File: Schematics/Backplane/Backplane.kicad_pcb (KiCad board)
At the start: 2 copper layers, 69.5 x 98.5 mm, 21 parts, among them J1 Edge Connector (SLOT 1), J2 Edge Connector (SLOT 2), J3 Edge Connector (SLOT 3), J4 Edge Connector (SLOT 4), J5 Edge Connector (SLOT 5), J6 Conn_01x06_Socket

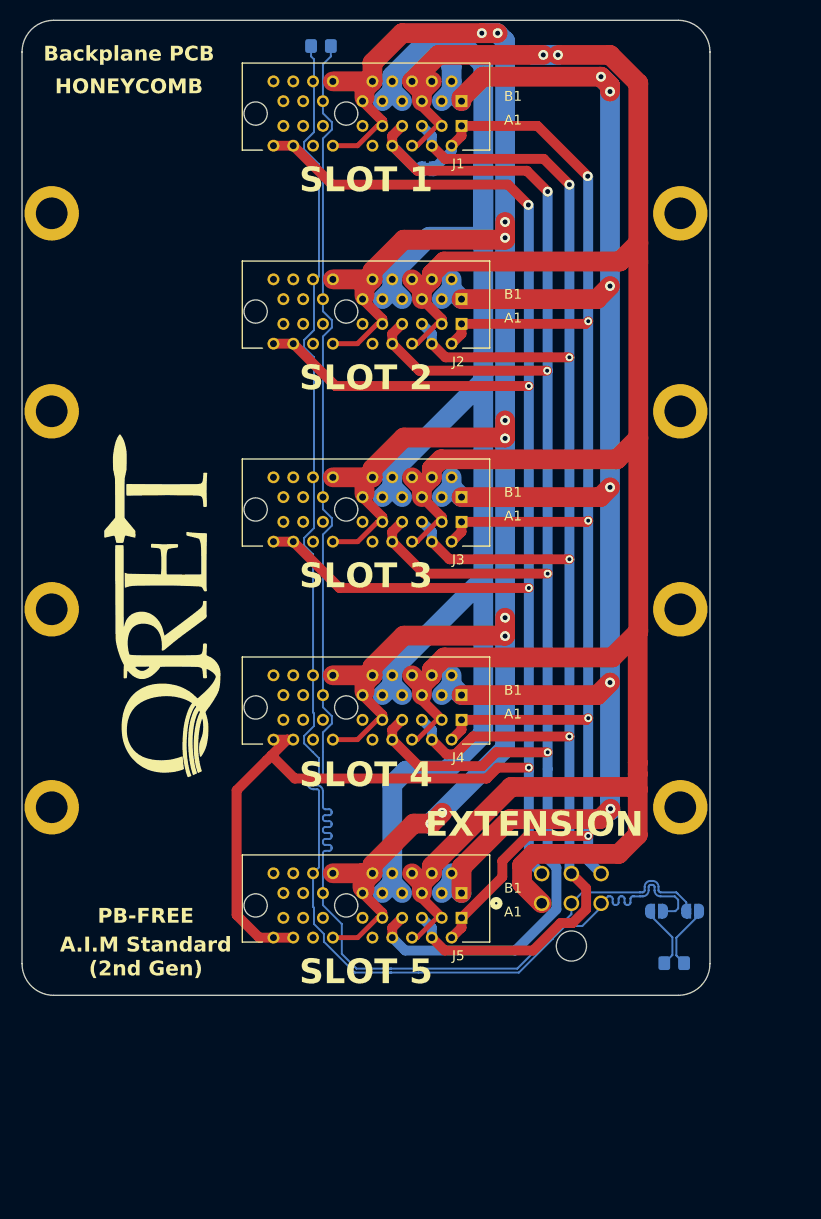
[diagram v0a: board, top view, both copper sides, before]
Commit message: restored non hybrid backplane
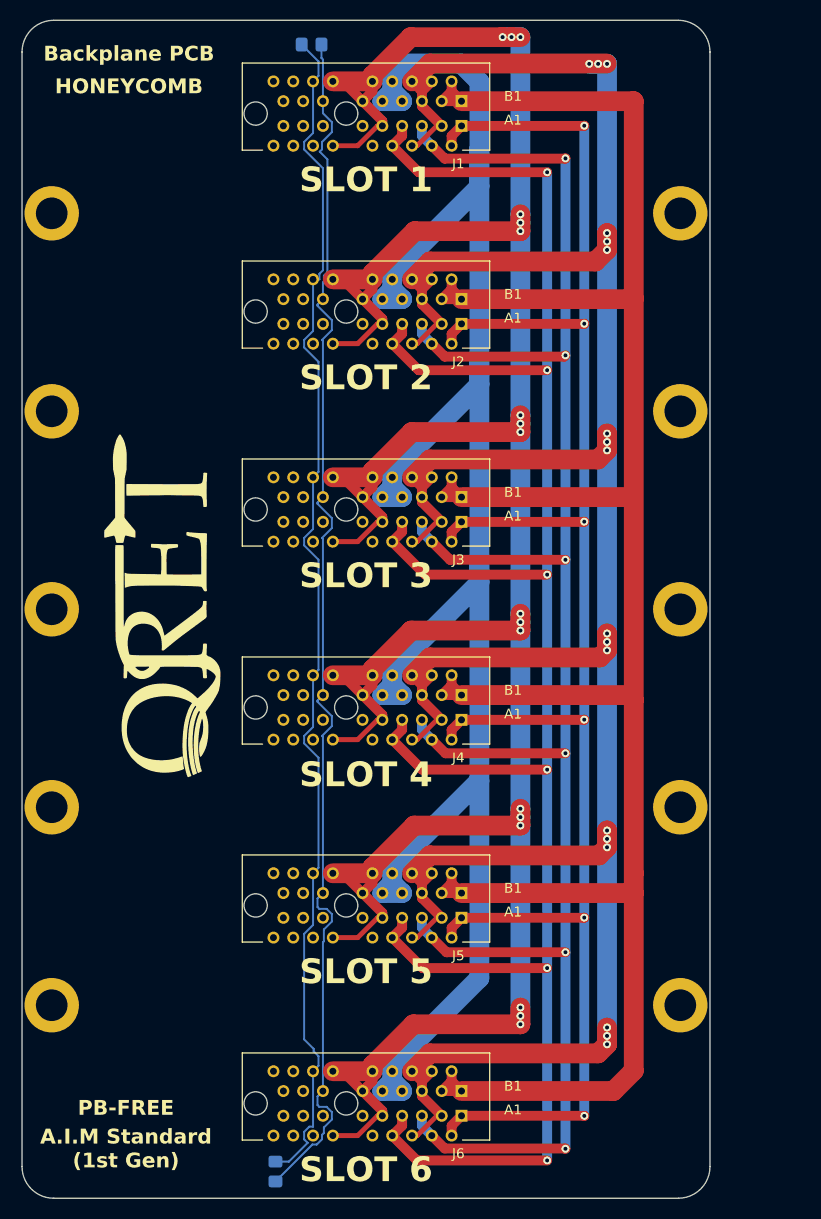
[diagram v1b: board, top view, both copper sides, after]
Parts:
- removed JP1, JP2: SolderJumper_2_Open, Jumper:SolderJumper-2_P1.3mm_Open_RoundedPad1.0x1.5mm
- removed JP3: 3.3V Bridge, Jumper:SolderJumper-2_P1.3mm_Bridged2Bar_RoundedPad1.0x1.5mm
- removed JP4: BATT Bridge, Jumper:SolderJumper-2_P1.3mm_Bridged2Bar_RoundedPad1.0x1.5mm
- removed JP5: GND Bridge, Jumper:SolderJumper-2_P1.3mm_Bridged2Bar_RoundedPad1.0x1.5mm
- added H10: MountingHole, MountingHole:MountingHole_3.2mm_M3_ISO14580_Pad, F.Cu at (66.5, 99.5)
- added H9: MountingHole, MountingHole:MountingHole_3.2mm_M3_ISO14580_Pad, F.Cu at (3.00, 99.5)
- J6: value Conn_01x06_Socket -> Edge Connector (SLOT 6); footprint footprints:CONN_SD-43045-001_06_MOL -> footprints:AMPHENOL_10018784-10210TLF; moved to F.Cu
- moved R2 45.4 mm to (25.6, 116.3), turned to -90 degrees
- moved J6 28.3 mm to (32.8, 109.4)
- moved R1 0.96 mm to (29.2, 2.45)
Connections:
- J1 pad A16: 24V_A -> unconnected-(J1-Reserved-PadA16)
- J1 pad A18: 24V_A -> unconnected-(J1-Reserved-PadA18)
- J1 pad B13: CAN_N -> CAN_L
- J1 pad B14: CAN_P -> CAN_H
- J2 pad A16: 24V_A -> unconnected-(J2-Reserved-PadA16)
- J2 pad A18: 24V_A -> unconnected-(J2-Reserved-PadA18)
- J2 pad B13: CAN_N -> CAN_L
- J2 pad B14: CAN_P -> CAN_H
- J3 pad A16: 24V_A -> unconnected-(J3-Reserved-PadA16)
- J3 pad A18: 24V_A -> unconnected-(J3-Reserved-PadA18)
- J3 pad B13: CAN_N -> CAN_L
- J3 pad B14: CAN_P -> CAN_H
- J4 pad A16: 24V_A -> unconnected-(J4-Reserved-PadA16)
- J4 pad A18: 24V_A -> unconnected-(J4-Reserved-PadA18)
- J4 pad B13: CAN_N -> CAN_L
- J4 pad B14: CAN_P -> CAN_H
- J5 pad A16: 24V_A -> unconnected-(J5-Reserved-PadA16)
- J5 pad A18: 24V_A -> unconnected-(J5-Reserved-PadA18)
- J5 pad B13: CAN_N -> CAN_L
- J5 pad B14: CAN_P -> CAN_H
- R1 pad 1: CAN_P -> CAN_H
- R1 pad 2: CAN_N -> CAN_L
- R2 pad 1: /TERM_P -> CAN_H
- R2 pad 2: /TERM_N -> CAN_L
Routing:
- net 24V_A: track 207.6 -> 0.00 mm, vias 4 -> 0
- net CAN_N: track 144.7 -> 0.00 mm
- net CAN_P: track 144.1 -> 0.00 mm
- net CAN_L: track 0.00 -> 125.7 mm
- net CAN_H: track 0.00 -> 123.4 mm
- net GND2: track 240.2 -> 329.8 mm, vias 10 -> 18
- net BATT_A: track 179.0 -> 237.6 mm, vias 6 -> 0
- net BATT_B: track 164.9 -> 212.4 mm
- net GND1: track 270.0 -> 311.8 mm, vias 2 -> 18
- net 3.3V_B: track 176.5 -> 215.4 mm, vias 4 -> 6
- net 5.0V_A: track 164.0 -> 199.2 mm, vias 4 -> 6
- net 3.3V_A: track 157.0 -> 189.0 mm, vias 5 -> 6
- net /TERM_N: track 6.55 -> 0.00 mm
- net /TERM_P: track 6.52 -> 0.00 mm
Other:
- board size 69.5 x 98.5 mm -> 69.5 x 119 mm
- board text added: "A.I.M Standard (1st Gen)"
- board text added: "Backplane PCB Rev 1.1 QRET Mar 2025 Kennan Bays Owen Price"
- board text added: "SLOT 6"
- board text removed: "A.I.M Standard (2nd Gen)"
- board text removed: "Backplane PCB Rev 1.2 QRET Mar 2026 Abigail Elms Kennan Bays Owen Price"
- board text removed: "EXTENSION"

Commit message: init commit of hybrid backplane with new extension connector  - using bridges to merge POWER trace B with A for altimter  - add 120ohm termination bridge to allow CAN to work standlone
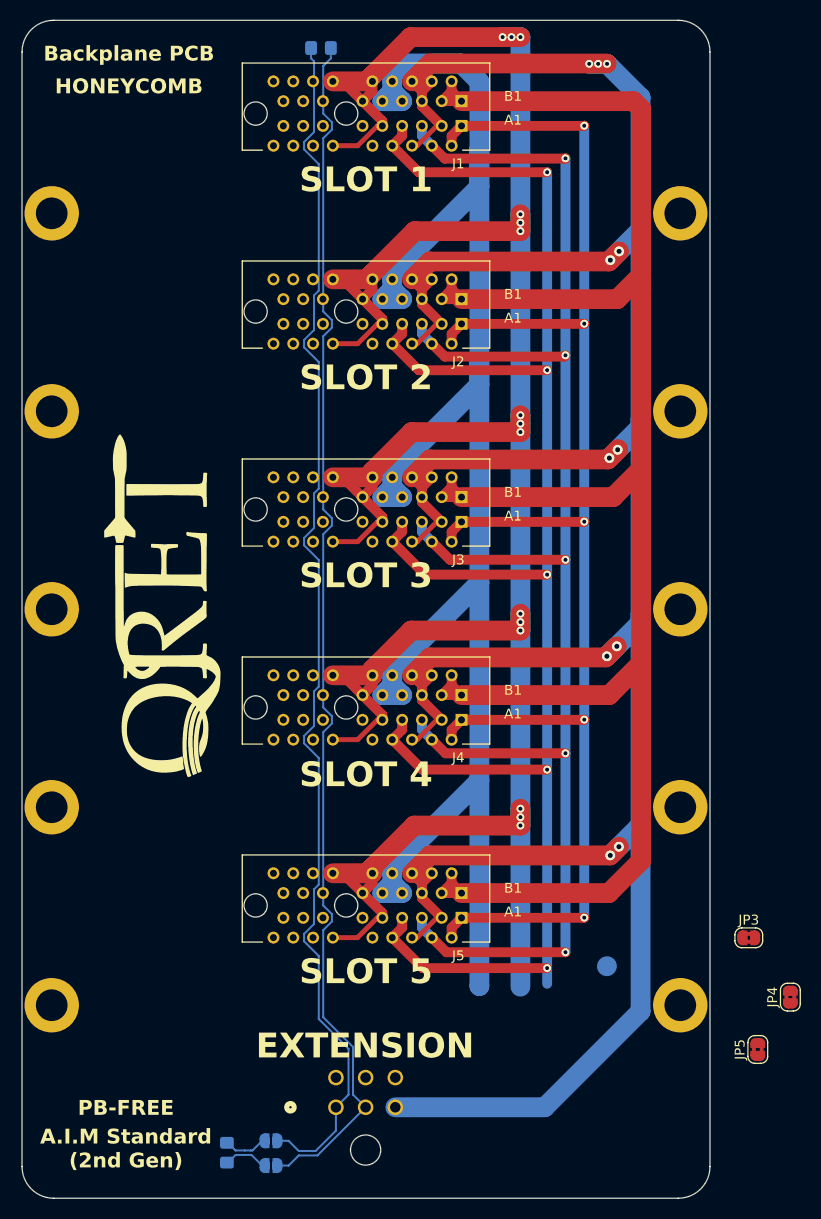
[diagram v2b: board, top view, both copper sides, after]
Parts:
- added JP1: SolderJumper_2_Open, Jumper:SolderJumper-2_P1.3mm_Open_RoundedPad1.0x1.5mm, B.Cu at (25.1, 115.7)
- added JP2: SolderJumper_2_Open, Jumper:SolderJumper-2_P1.3mm_Open_RoundedPad1.0x1.5mm, B.Cu at (25.1, 113.2)
- added JP3: SolderJumper_2_Bridged, Jumper:SolderJumper-2_P1.3mm_Bridged2Bar_RoundedPad1.0x1.5mm, F.Cu at (73.4, 92.7)
- added JP4: SolderJumper_2_Bridged, Jumper:SolderJumper-2_P1.3mm_Bridged2Bar_RoundedPad1.0x1.5mm, F.Cu at (77.6, 98.7)
- added JP5: SolderJumper_2_Bridged, Jumper:SolderJumper-2_P1.3mm_Bridged2Bar_RoundedPad1.0x1.5mm, F.Cu at (74.3, 104.0)
- J6: value Edge Connector (SLOT 6) -> Conn_01x06_Socket; footprint footprints:AMPHENOL_10018784-10210TLF -> footprints:CONN_SD-43045-001_06_MOL; moved to B.Cu
- moved R2 5.26 mm to (20.7, 114.4)
- moved J6 1.11 mm to (31.7, 109.8)
- moved R1 1.01 mm to (30.2, 2.80)
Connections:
- J1 pad A15: unconnected-(J1-Reserved-PadA15) -> 24V_A
- J1 pad A16: unconnected-(J1-Reserved-PadA16) -> 24V_A
- J1 pad A17: unconnected-(J1-Reserved-PadA17) -> 24V_A
- J1 pad A18: unconnected-(J1-Reserved-PadA18) -> 24V_A
- J1 pad B13: CAN_L -> CAN_N
- J1 pad B14: CAN_H -> CAN_P
- J1 pad B15: unconnected-(J1-Reserved-PadB15) -> GND1
- J1 pad B16: unconnected-(J1-Reserved-PadB16) -> GND1
- J1 pad B17: unconnected-(J1-Reserved-PadB17) -> GND1
- J1 pad B18: unconnected-(J1-Reserved-PadB18) -> GND1
- J2 pad A15: unconnected-(J2-Reserved-PadA15) -> 24V_A
- J2 pad A16: unconnected-(J2-Reserved-PadA16) -> 24V_A
- J2 pad A17: unconnected-(J2-Reserved-PadA17) -> 24V_A
- J2 pad A18: unconnected-(J2-Reserved-PadA18) -> 24V_A
- J2 pad B13: CAN_L -> CAN_N
- J2 pad B14: CAN_H -> CAN_P
- J2 pad B15: unconnected-(J2-Reserved-PadB15) -> GND1
- J2 pad B16: unconnected-(J2-Reserved-PadB16) -> GND1
- J2 pad B17: unconnected-(J2-Reserved-PadB17) -> GND1
- J2 pad B18: unconnected-(J2-Reserved-PadB18) -> GND1
- J3 pad A15: unconnected-(J3-Reserved-PadA15) -> 24V_A
- J3 pad A16: unconnected-(J3-Reserved-PadA16) -> 24V_A
- J3 pad A17: unconnected-(J3-Reserved-PadA17) -> 24V_A
- J3 pad A18: unconnected-(J3-Reserved-PadA18) -> 24V_A
- J3 pad B13: CAN_L -> CAN_N
- J3 pad B14: CAN_H -> CAN_P
- J3 pad B15: unconnected-(J3-Reserved-PadB15) -> GND1
- J3 pad B16: unconnected-(J3-Reserved-PadB16) -> GND1
- J3 pad B17: unconnected-(J3-Reserved-PadB17) -> GND1
- J3 pad B18: unconnected-(J3-Reserved-PadB18) -> GND1
- J4 pad A15: unconnected-(J4-Reserved-PadA15) -> 24V_A
- J4 pad A16: unconnected-(J4-Reserved-PadA16) -> 24V_A
- J4 pad A17: unconnected-(J4-Reserved-PadA17) -> 24V_A
- J4 pad A18: unconnected-(J4-Reserved-PadA18) -> 24V_A
- J4 pad B13: CAN_L -> CAN_N
- J4 pad B14: CAN_H -> CAN_P
- J4 pad B15: unconnected-(J4-Reserved-PadB15) -> GND1
- J4 pad B16: unconnected-(J4-Reserved-PadB16) -> GND1
- J4 pad B17: unconnected-(J4-Reserved-PadB17) -> GND1
- J4 pad B18: unconnected-(J4-Reserved-PadB18) -> GND1
- J5 pad A15: unconnected-(J5-Reserved-PadA15) -> 24V_A
- J5 pad A16: unconnected-(J5-Reserved-PadA16) -> 24V_A
- J5 pad A17: unconnected-(J5-Reserved-PadA17) -> 24V_A
- J5 pad A18: unconnected-(J5-Reserved-PadA18) -> 24V_A
- J5 pad B13: CAN_L -> CAN_N
- J5 pad B14: CAN_H -> CAN_P
- J5 pad B15: unconnected-(J5-Reserved-PadB15) -> GND1
- J5 pad B16: unconnected-(J5-Reserved-PadB16) -> GND1
- J5 pad B17: unconnected-(J5-Reserved-PadB17) -> GND1
- J5 pad B18: unconnected-(J5-Reserved-PadB18) -> GND1
- R1 pad 1: CAN_H -> CAN_P
- R1 pad 2: CAN_L -> CAN_N
- R2 pad 1: CAN_H -> /TERM_P
- R2 pad 2: CAN_L -> /TERM_N
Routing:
- net CAN_L: track 125.7 -> 0.00 mm
- net CAN_P: track 0.00 -> 124.4 mm
- net CAN_N: track 0.00 -> 124.1 mm
- net CAN_H: track 123.4 -> 0.00 mm
- net GND2: track 329.8 -> 287.2 mm, vias 18 -> 15
- net 3.3V_B: track 215.4 -> 178.4 mm, vias 6 -> 5
- net 5.0V_A: track 199.2 -> 162.9 mm, vias 6 -> 5
- net BATT_A: track 237.6 -> 202.6 mm
- net 3.3V_A: track 189.0 -> 154.1 mm, vias 6 -> 5
- net BATT_B: track 212.4 -> 191.8 mm
- net GND1: track 311.8 -> 320.6 mm, vias 18 -> 11
- net /TERM_N: track 0.00 -> 4.57 mm
- net /TERM_P: track 0.00 -> 4.52 mm
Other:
- board text added: "A.I.M Standard (2nd Gen)"
- board text added: "EXTENSION"
- board text removed: "A.I.M Standard (1st Gen)"
- board text removed: "SLOT 6"
